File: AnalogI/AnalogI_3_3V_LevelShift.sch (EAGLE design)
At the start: 78 parts, among them IC1 HCPL-7800, IC2 HCPL-7800, IC3 HCPL-7800, IC4 HCPL-7800, IC5 MCP3424SOIC, IC6 74HC4051_MUXN, IC7 74HC4051_MUXN, P1 DF11-06-2DSA, Q1 BS170, Q2 BS170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

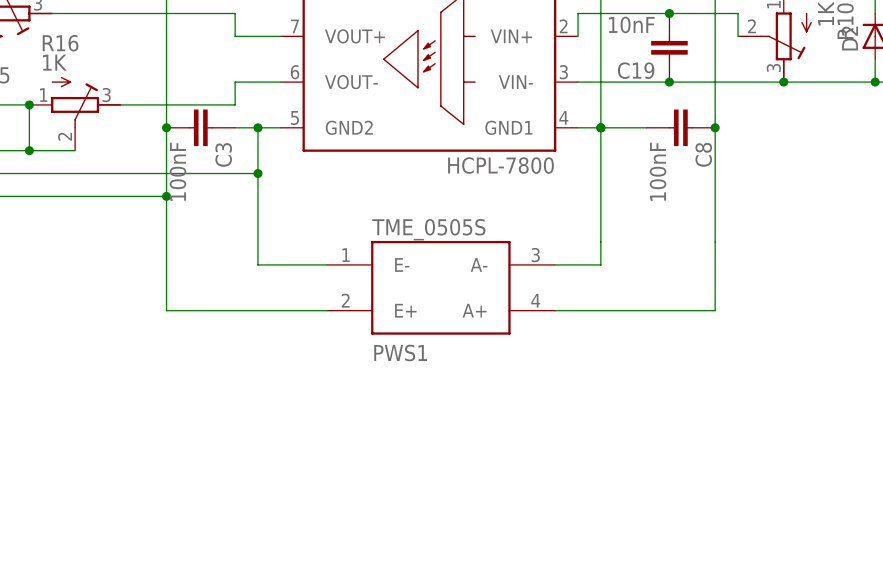
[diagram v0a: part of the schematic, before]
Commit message: Add capacitors on dc/dc isolator.
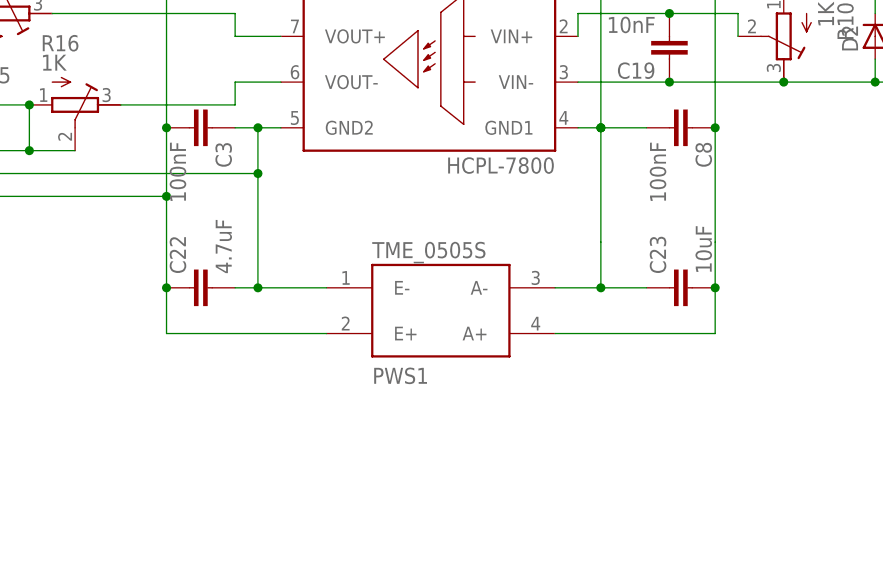
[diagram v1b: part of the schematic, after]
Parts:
- added C22: 4.7uF, rcl:C-EUC0805
- added C23: 10uF, rcl:C-EUC0805
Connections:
- net +5V: now also C22.1
- net GND: now also C22.2
- net N$33: now also C23.1
- net N$8: now also C23.2
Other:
- moved on the sheet: PWS1
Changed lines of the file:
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@@
 <part name="R36" library="rcl" deviceset="R-EU_" device="0204/2V" value="10K"/>
 <part name="R37" library="rcl" deviceset="R-EU_" device="0204/2V" value="10K"/>
+<part name="C23" library="rcl" deviceset="C-EU" device="C0805" value="10uF"/>
+<part name="C22" library="rcl" deviceset="C-EU" device="C0805" value="4.7uF"/>
 </parts>
 <sheets>
@@
 <instance part="X1" gate="G$1" x="246.38" y="17.78" rot="MR180"/>
 <instance part="X2" gate="G$1" x="-101.6" y="17.78" rot="R180"/>
-<instance part="PWS1" gate="G$1" x="177.8" y="-22.86" rot="MR180"/>
+<instance part="PWS1" gate="G$1" x="177.8" y="-25.4" rot="MR180"/>
 <instance part="R29" gate="G$1" x="48.26" y="5.08" rot="MR0"/>
 <instance part="R30" gate="G$1" x="53.34" y="0" rot="MR0"/>
@@
 <instance part="R36" gate="G$1" x="-73.66" y="43.18" rot="MR180"/>
 <instance part="R37" gate="G$1" x="-73.66" y="15.24" rot="MR180"/>
+<instance part="C23" gate="G$1" x="203.2" y="-22.86" rot="R90"/>
+<instance part="C22" gate="G$1" x="149.86" y="-22.86" rot="R90"/>
 </instances>
 <busses>
@@
 <junction x="104.14" y="-7.62"/>
 <wire x1="104.14" y1="0" x2="104.14" y2="-7.62" width="0.1524" layer="91"/>
-<wire x1="157.48" y1="-10.16" x2="157.48" y2="-20.32" width="0.1524" layer="91"/>
+<wire x1="157.48" y1="-10.16" x2="157.48" y2="-22.86" width="0.1524" layer="91"/>
 <pinref part="PWS1" gate="G$1" pin="E-"/>
-<wire x1="157.48" y1="-20.32" x2="165.1" y2="-20.32" width="0.1524" layer="91"/>
+<wire x1="157.48" y1="-22.86" x2="165.1" y2="-22.86" width="0.1524" layer="91"/>
 <junction x="157.48" y="-10.16"/>
 <pinref part="IC7" gate="G$1" pin="INH"/>
@@
 <wire x1="101.6" y1="0" x2="104.14" y2="0" width="0.1524" layer="91"/>
 <junction x="104.14" y="0"/>
+<pinref part="C22" gate="G$1" pin="2"/>
+<wire x1="157.48" y1="-22.86" x2="154.94" y2="-22.86" width="0.1524" layer="91"/>
+<junction x="157.48" y="-22.86"/>
 </segment>
 </net>
@@
 <junction x="83.82" y="-12.7"/>
 <junction x="147.32" y="-5.08"/>
-<wire x1="147.32" y1="-12.7" x2="147.32" y2="-25.4" width="0.1524" layer="91"/>
+<wire x1="147.32" y1="-12.7" x2="147.32" y2="-17.78" width="0.1524" layer="91"/>
 <pinref part="PWS1" gate="G$1" pin="E+"/>
-<wire x1="147.32" y1="-25.4" x2="165.1" y2="-25.4" width="0.1524" layer="91"/>
+<wire x1="147.32" y1="-17.78" x2="147.32" y2="-22.86" width="0.1524" layer="91"/>
+<wire x1="147.32" y1="-22.86" x2="147.32" y2="-27.94" width="0.1524" layer="91"/>
+<wire x1="147.32" y1="-27.94" x2="165.1" y2="-27.94" width="0.1524" layer="91"/>
 <junction x="147.32" y="-12.7"/>
 <wire x1="0" y1="-12.7" x2="-33.02" y2="-12.7" width="0.1524" layer="91"/>
@@
 <junction x="91.44" y="-25.4"/>
 <junction x="91.44" y="-27.94"/>
+<pinref part="C22" gate="G$1" pin="1"/>
+<junction x="147.32" y="-22.86"/>
 </segment>
 </net>
@@
 <junction x="208.28" y="38.1"/>
 <pinref part="PWS1" gate="G$1" pin="A+"/>
-<wire x1="190.5" y1="-25.4" x2="208.28" y2="-25.4" width="0.1524" layer="91"/>
-<wire x1="208.28" y1="-25.4" x2="208.28" y2="-17.78" width="0.1524" layer="91"/>
+<wire x1="190.5" y1="-27.94" x2="208.28" y2="-27.94" width="0.1524" layer="91"/>
+<wire x1="208.28" y1="-27.94" x2="208.28" y2="-22.86" width="0.1524" layer="91"/>
 <junction x="208.28" y="-5.08"/>
+<wire x1="208.28" y1="-22.86" x2="208.28" y2="-17.78" width="0.1524" layer="91"/>
 <wire x1="208.28" y1="-17.78" x2="208.28" y2="-5.08" width="0.1524" layer="91"/>
+<pinref part="C23" gate="G$1" pin="2"/>
+<junction x="208.28" y="-22.86"/>
 </segment>
 </net>
@@
 <wire x1="193.04" y1="-5.08" x2="195.58" y2="-5.08" width="0.1524" layer="91"/>
 <pinref part="PWS1" gate="G$1" pin="A-"/>
-<wire x1="190.5" y1="-20.32" x2="195.58" y2="-20.32" width="0.1524" layer="91"/>
-<wire x1="195.58" y1="-20.32" x2="195.58" y2="-17.78" width="0.1524" layer="91"/>
+<wire x1="190.5" y1="-22.86" x2="195.58" y2="-22.86" width="0.1524" layer="91"/>
+<wire x1="195.58" y1="-22.86" x2="195.58" y2="-17.78" width="0.1524" layer="91"/>
 <junction x="195.58" y="-5.08"/>
 <pinref part="C9" gate="G$1" pin="2"/>
@@
 <wire x1="-48.26" y1="22.86" x2="-48.26" y2="-5.08" width="0.1524" layer="91"/>
 <junction x="-48.26" y="-5.08"/>
-</segment>
-</net>
+<pinref part="C23" gate="G$1" pin="1"/>
+<wire x1="195.58" y1="-22.86" x2="200.66" y2="-22.86" width="0.1524" layer="91"/>
+<junction x="195.58" y="-22.86"/>
+</segment>
+</net>
